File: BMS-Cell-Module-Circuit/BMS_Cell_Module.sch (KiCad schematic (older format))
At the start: 32 parts, among them J1 Conn_01x02_Female, J2 Conn_01x04_Female, J3 Conn_01x04_Female, M1 SI2312BDS-T1-E3, U2 ADUM1250ARZ, U3 ATTINY85V-10SU 8S2 EIAJ SOIC

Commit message: First check in
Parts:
- removed M1: SI2312BDS-T1-E3, TO_SOT_Packages_SMD:SOT-23, symbol BMS_Cell_Module-rescue:SI2312BDS-T1-E3
- removed R5: 47K, Resistors_SMD:R_1206_HandSoldering, symbol Device:R
- added Q1: SI2312BDS-T1-E3, Package_TO_SOT_SMD:SOT-23, symbol Device:Q_NMOS_GSD
- C1, C2: value 2.2uF Ceramic X7R -> 2.2uF; footprint Capacitors_SMD:C_1206_HandSoldering -> Capacitor_SMD:C_0805_2012Metric_Pad1.33x1.40mm_HandSolder
- C3, C4, C5: footprint Capacitors_SMD:C_1206_HandSoldering -> Capacitor_SMD:C_0805_2012Metric_Pad1.33x1.40mm_HandSolder
- C6: value 0.22uF Ceramic X7R -> 0.22uF; footprint Capacitors_SMD:C_1206_HandSoldering -> Capacitor_SMD:C_0805_2012Metric_Pad1.33x1.40mm_HandSolder
- D1: value SS34 Schottky Rectifier, 40 V, 3 A -> SS34 Schottky 40V/3A
- D2, D4: footprint LEDs:LED_1206_HandSoldering -> LED_SMD:LED_0805_2012Metric_Pad1.15x1.40mm_HandSolder
- F1: footprint Resistors_SMD:R_1812_HandSoldering -> Resistor_SMD:R_1812_4532Metric_Pad1.42x3.40mm_HandSolder
- ISP1: symbol conn:Conn_02x03_Odd_Even -> Connector_Generic:Conn_02x03_Odd_Even
- J1: symbol conn:Conn_01x02_Female -> Connector:Conn_01x02_Female
- J2, J3: symbol conn:Conn_01x04_Female -> Connector:Conn_01x04_Female
- R1: value HS50 3R3 J 50W Axial Wire Wound -> 2R/10W
- R10, R12, R8: value 2K2 -> 4K7; footprint Resistors_SMD:R_1206_HandSoldering -> Resistor_SMD:R_0805_2012Metric_Pad1.33x1.40mm_HandSolder
- R2: value 47R -> 4K7; footprint Resistors_SMD:R_1206_HandSoldering -> Resistor_SMD:R_0805_2012Metric_Pad1.33x1.40mm_HandSolder
- R3, R4, R7, R9: footprint Resistors_SMD:R_1206_HandSoldering -> Resistor_SMD:R_0805_2012Metric_Pad1.33x1.40mm_HandSolder
- R6: value 470K -> 510K; footprint Resistors_SMD:R_1206_HandSoldering -> Resistor_SMD:R_0805_2012Metric_Pad1.33x1.40mm_HandSolder
- TP1, TP2: footprint Connectors:PINTST -> TestPoint:TestPoint_Pad_D1.5mm; symbol BMS_Cell_Module-rescue:TEST -> Connector:TestPoint
- U2: footprint adum1250:ADUM1250 -> Package_SO:SOIC-8_3.9x4.9mm_P1.27mm
- U3: footprint ATTINY:ATTINY85V -> Package_SO:SOIJ-8_5.3x5.3mm_P1.27mm; symbol atmel:ATTINY85-20SU -> MCU_Microchip_ATtiny:ATtiny85-20SU
- renumbered R11 to U1
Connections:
- net labels added: MOSI, RST
- net labels removed: RESET, SDA
- wire segments 154 -> 156
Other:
- note added: "2-channel bidirectional digital isolator\nfor external I2C bus\n(can replace with ISO1540DR)"
- note added: "Battery voltage divider\n1.8→4.5V maps to\nADC3=1.029V→2.571V"
- note added: "C1/C2/C6 ceramic, X7R or X5R"
- note added: "Li-Ion battery input\n1.8→4.5V"
- note added: "N-channel MOSFET"
- note added: "Power resistor 10→50W"
- note added: "drain"
- note added: "gate"
- note added: "side 1\nstrict I2C"
- note added: "side 2\nrelaxed I2C"
- note added: "source"
- note removed: "BMS Cell Module for Lithium Cells\nStuart Pittaway\n\nInspired by LyteFyba BMS by weber and Coulomb"
- note removed: "For C1/C2/C6 Surface-mount ceramic types. \nIn all cases, X7R or X5R dielectric are recommended."
- note removed: "Input battery voltage resistor \ndivider 517K vs 680K\n4.5V maps to 2.55V"
- note removed: "LiOn Battery measuring \nvoltage range 2.7V to 4.35V"
- note removed: "Thermistor into ADC0 \n(RESET PIN) must not go \nbelow VCC/2 or reset is forced"
- moved on the sheet: C4, C5, D4, R10, R12, R8, R9, U2, U3

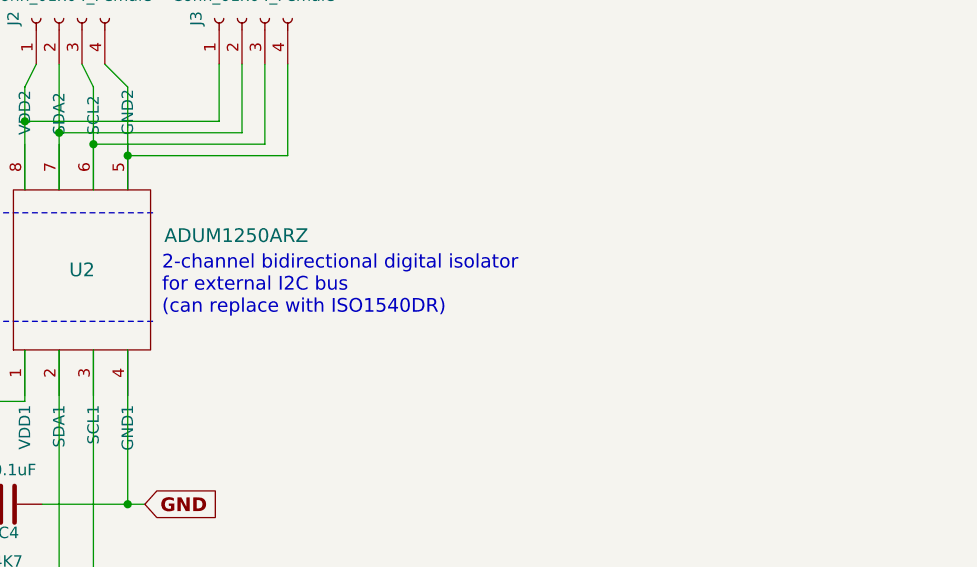
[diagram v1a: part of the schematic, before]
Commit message: Removed URLs for incorrect sized compontents
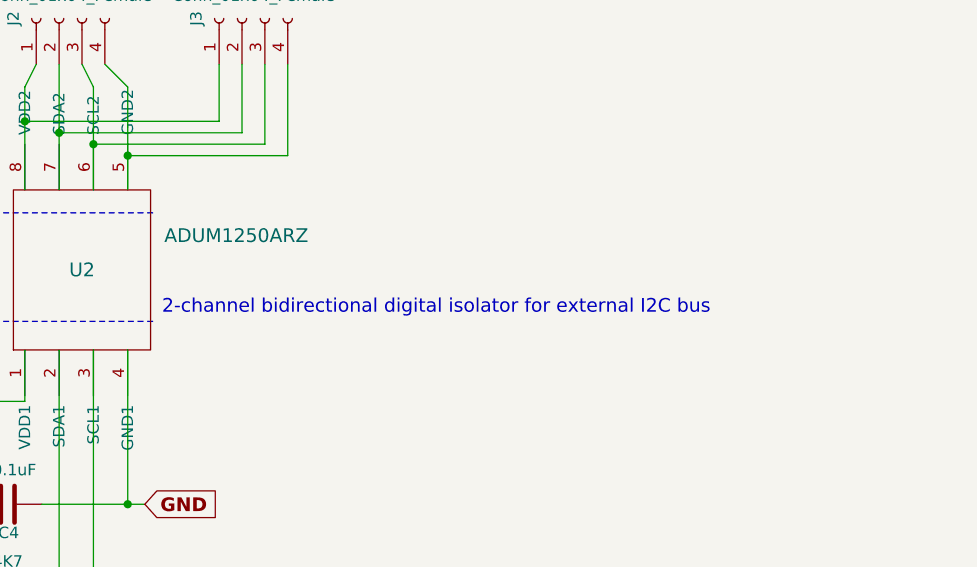
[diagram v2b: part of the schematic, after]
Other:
- note added: "2-channel bidirectional digital isolator for external I2C bus\n"
- note removed: "2-channel bidirectional digital isolator\nfor external I2C bus\n(can replace with ISO1540DR)"
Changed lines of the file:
@@
 F 1 "2.2uF" H 1640 3700 50  0000 L CNN
 F 2 "Capacitor_SMD:C_0805_2012Metric_Pad1.33x1.40mm_HandSolder" H 1578 3550 50  0001 C CNN
-F 3 "http://uk.farnell.com/kemet/c1206x224k5ractu/cap-mlcc-x7r-220nf-50v-1206/dp/1414056" H 1540 3700 50  0001 C CNN
+F 3 "" H 1540 3700 50  0001 C CNN
 	1    1540 3700
 	1    0    0    -1
@@
 F 1 "2.2uF" H 3360 4500 50  0000 L CNN
 F 2 "Capacitor_SMD:C_0805_2012Metric_Pad1.33x1.40mm_HandSolder" H 3268 4340 50  0001 C CNN
-F 3 "http://uk.farnell.com/kemet/c1206x224k5ractu/cap-mlcc-x7r-220nf-50v-1206/dp/1414056" H 3230 4490 50  0001 C CNN
+F 3 "" H 3230 4490 50  0001 C CNN
 	1    3230 4490
 	1    0    0    -1
@@
 F 1 "2R/10W" V 2200 6850 50  0000 C CNN
 F 2 "Resistors_THT:R_Axial_Power_L50.0mm_W9.0mm_P60.96mm" V 2230 6850 50  0001 C CNN
-F 3 "http://uk.rs-online.com/web/p/panel-mount-fixed-resistors/0160916/" H 2300 6850 50  0001 C CNN
+F 3 "" H 2300 6850 50  0001 C CNN
 	1    2300 6850
 	0    1    1    0
@@
 F 1 "0.22uF" H 3320 3810 50  0000 L CNN
 F 2 "Capacitor_SMD:C_0805_2012Metric_Pad1.33x1.40mm_HandSolder" H 3318 3750 50  0001 C CNN
-F 3 "http://uk.farnell.com/kemet/c1206x224k5ractu/cap-mlcc-x7r-220nf-50v-1206/dp/1414056" H 3280 3900 50  0001 C CNN
+F 3 "" H 3280 3900 50  0001 C CNN
 	1    3280 3900
 	1    0    0    -1
@@
 Connection ~ 4550 7050
 Text Notes 6500 2400 0    60   ~ 0
-2-channel bidirectional digital isolator\nfor external I2C bus\n(can replace with ISO1540DR)
+2-channel bidirectional digital isolator for external I2C bus\n
 Text Notes 5275 2625 0    60   ~ 0
 side 1\nstrict I2C

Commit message: Update BOM
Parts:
- C5: value 0.1uF -> 0.1uF polarized
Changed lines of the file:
@@
 P 8370 5050
 F 0 "C5" H 8395 5150 50  0000 L CNN
-F 1 "0.1uF" H 8395 4950 50  0000 L CNN
+F 1 "0.1uF polarized" H 8000 4900 50  0000 L CNN
 F 2 "Capacitor_SMD:C_0805_2012Metric_Pad1.33x1.40mm_HandSolder" H 8408 4900 50  0001 C CNN
 F 3 "" H 8370 5050 50  0001 C CNN
